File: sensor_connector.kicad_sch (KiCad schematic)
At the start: 4 parts

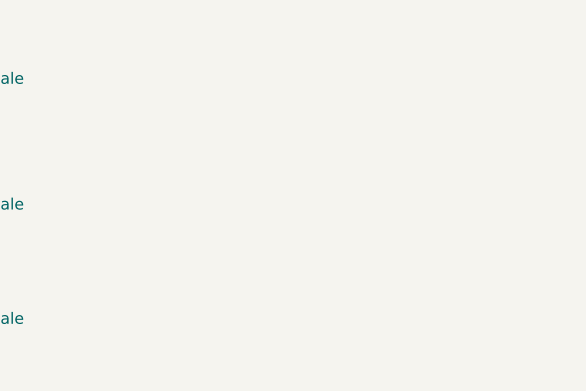
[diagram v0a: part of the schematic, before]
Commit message: Added Amplifier board om "special" lib. Added Amplifier to board with shutdown pins. Added DHT11 sensor to sensor schematic. Updated connector lib.
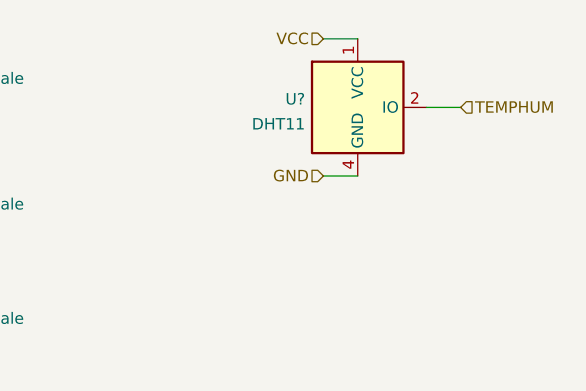
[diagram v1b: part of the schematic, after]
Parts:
- added U?: DHT11, Sensor:Aosong_DHT11_5.5x12.0_P2.54mm, symbol Sensor:DHT11
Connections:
- net GND: now also U?.4 (GND)
- net VCC: now also U?.1 (VCC)
- new net TEMPHUM: U?.2 (IO)
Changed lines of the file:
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@@
 (kicad_sch (version 20211123) (generator eeschema)
   (paper "A4")
+  (wire (pts (xy 156.21 54.61) (xy 152.4 54.61))
+    (stroke (width 0) (type default) (color 0 0 0 0))
+  )
   (wire (pts (xy 83.82 60.96) (xy 80.01 60.96))
     (stroke (width 0) (type default) (color 0 0 0 0))
@@
   )
   (wire (pts (xy 80.01 63.5) (xy 83.82 63.5))
+    (stroke (width 0) (type default) (color 0 0 0 0))
+  )
+  (wire (pts (xy 144.78 62.23) (xy 140.97 62.23))
     (stroke (width 0) (type default) (color 0 0 0 0))
   )
@@
     (stroke (width 0) (type default) (color 0 0 0 0))
   )
+  (wire (pts (xy 144.78 46.99) (xy 140.97 46.99))
+    (stroke (width 0) (type default) (color 0 0 0 0))
+  )
   (hierarchical_label "GND" (shape input) (at 80.01 78.74 180)
     (effects (font (size 1.27 1.27)) (justify right))
@@
   )
   (hierarchical_label "GND" (shape input) (at 80.01 66.04 180)
+    (effects (font (size 1.27 1.27)) (justify right))
+  )
+  (hierarchical_label "VCC" (shape input) (at 140.97 46.99 180)
+    (effects (font (size 1.27 1.27)) (justify right))
+  )
+  (hierarchical_label "TEMPHUM" (shape input) (at 156.21 54.61 0)
+    (effects (font (size 1.27 1.27)) (justify left))
+  )
+  (hierarchical_label "GND" (shape input) (at 140.97 62.23 180)
     (effects (font (size 1.27 1.27)) (justify right))
   )
@@
     (pin "3")
   )
+  (symbol (lib_id "Sensor:DHT11") (at 144.78 54.61 0) (unit 1)
+    (in_bom yes) (on_board yes) (fields_autoplaced)
+    (property "Reference" "U?" (id 0) (at 138.9381 53.7015 0)
+      (effects (font (size 1.27 1.27)) (justify right))
+    )
+    (property "Value" "DHT11" (id 1) (at 138.9381 56.4766 0)
+      (effects (font (size 1.27 1.27)) (justify right))
+    )
+    (property "Footprint" "Sensor:Aosong_DHT11_5.5x12.0_P2.54mm" (id 2) (at 144.78 64.77 0)
+      (effects (font (size 1.27 1.27)) hide)
+    )
+    (property "Datasheet" "http://akizukidenshi.com/download/ds/aosong/DHT11.pdf" (id 3) (at 148.59 48.26 0)
+      (effects (font (size 1.27 1.27)) hide)
+    )
+    (pin "1")
+    (pin "2")
+    (pin "3")
+    (pin "4")
+  )
   (symbol (lib_id "Connector:Conn_01x03_Female") (at 88.9 63.5 0) (unit 1)

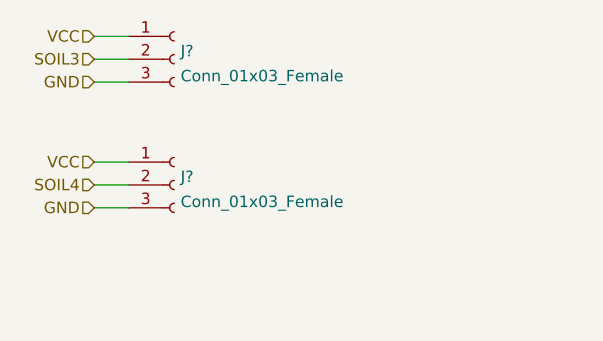
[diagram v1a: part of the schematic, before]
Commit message: Corrected RESET curcit to not keep the device in reset state. Added more capacitors to be a buffer for the motor. Added fuse to motor.
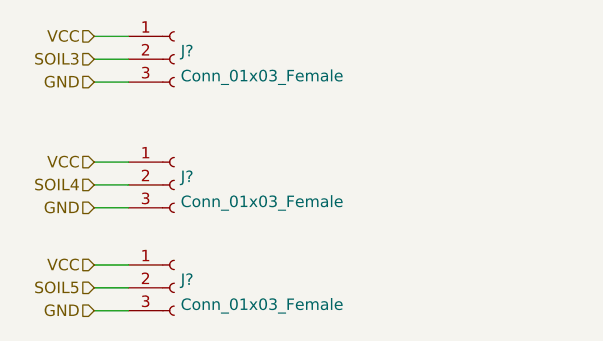
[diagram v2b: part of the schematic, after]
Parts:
- added J?: Conn_01x03_Female, symbol Connector:Conn_01x03_Female
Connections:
- net GND: now also J?.3 (Pin_3)
- net VCC: now also J?.1 (Pin_1)
- new net SOIL5: J?.2 (Pin_2)
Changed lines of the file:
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@@
+    (stroke (width 0) (type default) (color 0 0 0 0))
+  )
+  (wire (pts (xy 83.82 99.06) (xy 80.01 99.06))
     (stroke (width 0) (type default) (color 0 0 0 0))
   )
   (wire (pts (xy 80.01 63.5) (xy 83.82 63.5))
+    (stroke (width 0) (type default) (color 0 0 0 0))
+  )
+  (wire (pts (xy 83.82 104.14) (xy 80.01 104.14))
     (stroke (width 0) (type default) (color 0 0 0 0))
   )
@@
     (stroke (width 0) (type default) (color 0 0 0 0))
   )
+  (wire (pts (xy 80.01 101.6) (xy 83.82 101.6))
+    (stroke (width 0) (type default) (color 0 0 0 0))
+  )
   (wire (pts (xy 80.01 76.2) (xy 83.82 76.2))
     (stroke (width 0) (type default) (color 0 0 0 0))
@@
   (wire (pts (xy 144.78 46.99) (xy 140.97 46.99))
     (stroke (width 0) (type default) (color 0 0 0 0))
+  )
+  (hierarchical_label "SOIL5" (shape input) (at 80.01 101.6 180)
+    (effects (font (size 1.27 1.27)) (justify right))
   )
   (hierarchical_label "GND" (shape input) (at 80.01 78.74 180)
@@
     (effects (font (size 1.27 1.27)) (justify right))
   )
+  (hierarchical_label "VCC" (shape input) (at 80.01 99.06 180)
+    (effects (font (size 1.27 1.27)) (justify right))
+  )
   (hierarchical_label "GND" (shape input) (at 80.01 52.07 180)
     (effects (font (size 1.27 1.27)) (justify right))
   )
   (hierarchical_label "VCC" (shape input) (at 80.01 73.66 180)
+    (effects (font (size 1.27 1.27)) (justify right))
+  )
+  (hierarchical_label "GND" (shape input) (at 80.01 104.14 180)
     (effects (font (size 1.27 1.27)) (justify right))
   )
@@
       (effects (font (size 1.27 1.27)) hide)
     )
+    (pin "1")
+    (pin "2")
+    (pin "3")
+  )
+  (symbol (lib_id "Connector:Conn_01x03_Female") (at 88.9 101.6 0) (unit 1)
+    (in_bom yes) (on_board yes) (fields_autoplaced)
+    (property "Reference" "J?" (id 0) (at 89.6112 100.6915 0)
+      (effects (font (size 1.27 1.27)) (justify left))
+    )
+    (property "Value" "Conn_01x03_Female" (id 1) (at 89.6112 103.4666 0)
+      (effects (font (size 1.27 1.27)) (justify left))
+    )
+    (property "Footprint" "" (id 2) (at 88.9 101.6 0)
+      (effects (font (size 1.27 1.27)) hide)
+    )
+    (property "Datasheet" "~" (id 3) (at 88.9 101.6 0)
+      (effects (font (size 1.27 1.27)) hide)
+    )

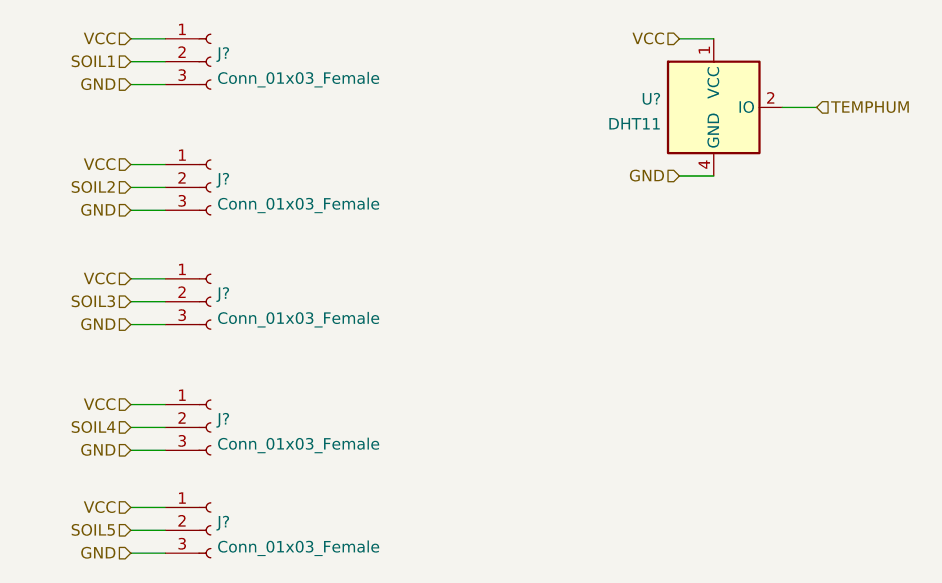
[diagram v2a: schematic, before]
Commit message: Added pcb, not routed but sorted. Gave all footprints refernces. Missing some footprints or might be wrong.
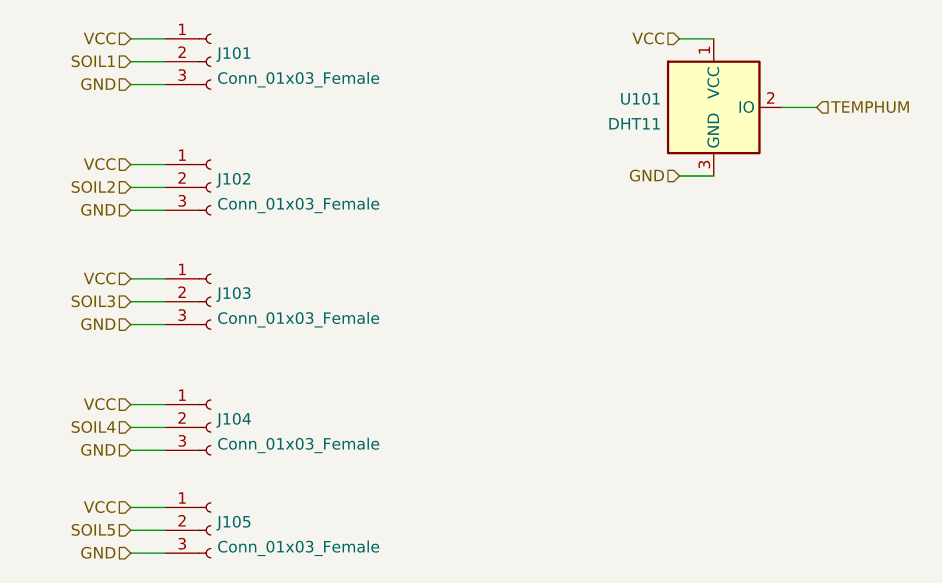
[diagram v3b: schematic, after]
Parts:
- J101, J102, J103, J104, J105: renamed from J?; footprint (none) -> Connector_JST:JST_XH_B3B-XH-A_1x03_P2.50mm_Vertical
- U101: renamed from U?; footprint Sensor:Aosong_DHT11_5.5x12.0_P2.54mm -> Connector_PinSocket_2.54mm:PinSocket_1x03_P2.54mm_Vertical; symbol Sensor:DHT11 -> special:DHT11
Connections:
- net GND: now also U101.3 (GND); no longer U101.4 (GND)
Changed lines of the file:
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@@
   (symbol (lib_id "Connector:Conn_01x03_Female") (at 88.9 90.17 0) (unit 1)
     (in_bom yes) (on_board yes) (fields_autoplaced)
-    (property "Reference" "J?" (id 0) (at 89.6112 89.2615 0)
+    (property "Reference" "J104" (id 0) (at 89.6112 89.2615 0)
       (effects (font (size 1.27 1.27)) (justify left))
     )
@@
       (effects (font (size 1.27 1.27)) (justify left))
     )
-    (property "Footprint" "" (id 2) (at 88.9 90.17 0)
+    (property "Footprint" "Connector_JST:JST_XH_B3B-XH-A_1x03_P2.50mm_Vertical" (id 2) (at 88.9 90.17 0)
       (effects (font (size 1.27 1.27)) hide)
     )
@@
   (symbol (lib_id "Connector:Conn_01x03_Female") (at 88.9 101.6 0) (unit 1)
     (in_bom yes) (on_board yes) (fields_autoplaced)
-    (property "Reference" "J?" (id 0) (at 89.6112 100.6915 0)
+    (property "Reference" "J105" (id 0) (at 89.6112 100.6915 0)
       (effects (font (size 1.27 1.27)) (justify left))
     )
@@
       (effects (font (size 1.27 1.27)) (justify left))
     )
-    (property "Footprint" "" (id 2) (at 88.9 101.6 0)
+    (property "Footprint" "Connector_JST:JST_XH_B3B-XH-A_1x03_P2.50mm_Vertical" (id 2) (at 88.9 101.6 0)
       (effects (font (size 1.27 1.27)) hide)
     )
@@
     (pin "3")
   )
-  (symbol (lib_id "Sensor:DHT11") (at 144.78 54.61 0) (unit 1)
+  (symbol (lib_id "special:DHT11") (at 144.78 54.61 0) (unit 1)
     (in_bom yes) (on_board yes) (fields_autoplaced)
-    (property "Reference" "U?" (id 0) (at 138.9381 53.7015 0)
+    (property "Reference" "U101" (id 0) (at 138.9381 53.7015 0)
       (effects (font (size 1.27 1.27)) (justify right))
     )
@@
       (effects (font (size 1.27 1.27)) (justify right))
     )
-    (property "Footprint" "Sensor:Aosong_DHT11_5.5x12.0_P2.54mm" (id 2) (at 144.78 64.77 0)
+    (property "Footprint" "Connector_PinSocket_2.54mm:PinSocket_1x03_P2.54mm_Vertical" (id 2) (at 144.78 64.77 0)
       (effects (font (size 1.27 1.27)) hide)
     )
@@
     (pin "2")
     (pin "3")
-    (pin "4")
   )
   (symbol (lib_id "Connector:Conn_01x03_Female") (at 88.9 63.5 0) (unit 1)
     (in_bom yes) (on_board yes) (fields_autoplaced)
-    (property "Reference" "J?" (id 0) (at 89.6112 62.5915 0)
+    (property "Reference" "J102" (id 0) (at 89.6112 62.5915 0)
       (effects (font (size 1.27 1.27)) (justify left))
     )
@@
       (effects (font (size 1.27 1.27)) (justify left))
     )
-    (property "Footprint" "" (id 2) (at 88.9 63.5 0)
+    (property "Footprint" "Connector_JST:JST_XH_B3B-XH-A_1x03_P2.50mm_Vertical" (id 2) (at 88.9 63.5 0)
       (effects (font (size 1.27 1.27)) hide)
     )
@@
   (symbol (lib_id "Connector:Conn_01x03_Female") (at 88.9 76.2 0) (unit 1)
     (in_bom yes) (on_board yes) (fields_autoplaced)
-    (property "Reference" "J?" (id 0) (at 89.6112 75.2915 0)
+    (property "Reference" "J103" (id 0) (at 89.6112 75.2915 0)
       (effects (font (size 1.27 1.27)) (justify left))
     )
@@
       (effects (font (size 1.27 1.27)) (justify left))
     )
-    (property "Footprint" "" (id 2) (at 88.9 76.2 0)
+    (property "Footprint" "Connector_JST:JST_XH_B3B-XH-A_1x03_P2.50mm_Vertical" (id 2) (at 88.9 76.2 0)
       (effects (font (size 1.27 1.27)) hide)
     )
@@
   (symbol (lib_id "Connector:Conn_01x03_Female") (at 88.9 49.53 0) (unit 1)
     (in_bom yes) (on_board yes) (fields_autoplaced)
-    (property "Reference" "J?" (id 0) (at 89.6112 48.6215 0)
+    (property "Reference" "J101" (id 0) (at 89.6112 48.6215 0)
       (effects (font (size 1.27 1.27)) (justify left))
     )
@@
       (effects (font (size 1.27 1.27)) (justify left))
     )
-    (property "Footprint" "" (id 2) (at 88.9 49.53 0)
+    (property "Footprint" "Connector_JST:JST_XH_B3B-XH-A_1x03_P2.50mm_Vertical" (id 2) (at 88.9 49.53 0)
       (effects (font (size 1.27 1.27)) hide)
     )

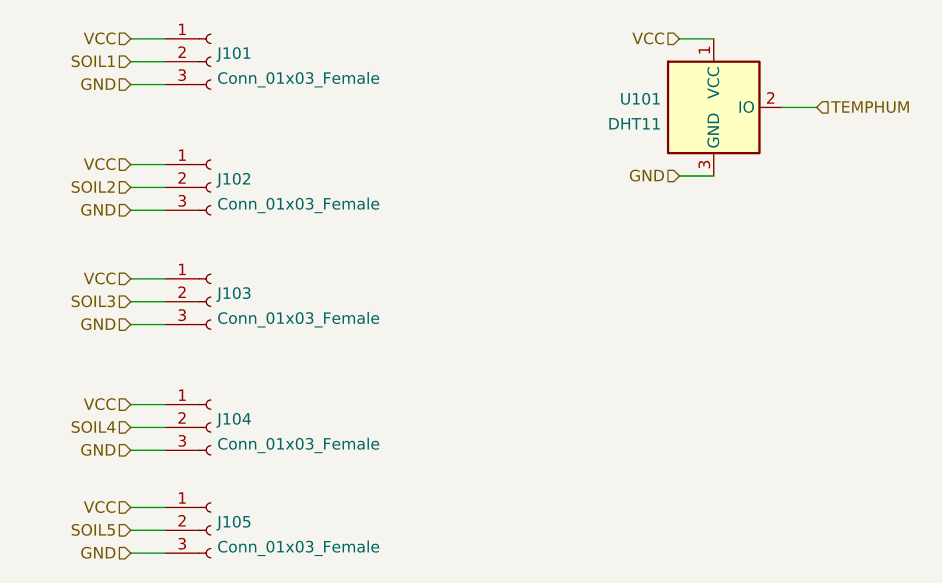
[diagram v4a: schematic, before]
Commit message: Renamed ConnectorEsp folder so 3D models work. Started routing and more layout work.
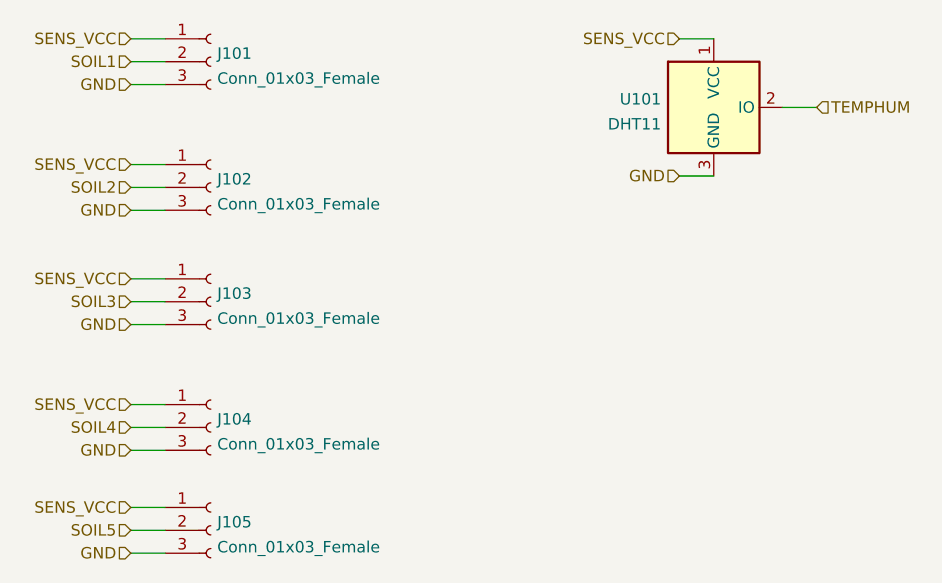
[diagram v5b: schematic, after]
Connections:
- net VCC renamed SENS_VCC
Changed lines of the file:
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@@
     (effects (font (size 1.27 1.27)) (justify right))
   )
-  (hierarchical_label "VCC" (shape input) (at 80.01 99.06 180)
+  (hierarchical_label "SENS_VCC" (shape input) (at 80.01 99.06 180)
     (effects (font (size 1.27 1.27)) (justify right))
   )
@@
     (effects (font (size 1.27 1.27)) (justify right))
   )
-  (hierarchical_label "VCC" (shape input) (at 80.01 73.66 180)
+  (hierarchical_label "SENS_VCC" (shape input) (at 80.01 73.66 180)
     (effects (font (size 1.27 1.27)) (justify right))
   )
@@
     (effects (font (size 1.27 1.27)) (justify right))
   )
-  (hierarchical_label "VCC" (shape input) (at 140.97 46.99 180)
+  (hierarchical_label "SENS_VCC" (shape input) (at 140.97 46.99 180)
     (effects (font (size 1.27 1.27)) (justify right))
   )
@@
     (effects (font (size 1.27 1.27)) (justify right))
   )
-  (hierarchical_label "VCC" (shape input) (at 80.01 87.63 180)
+  (hierarchical_label "SENS_VCC" (shape input) (at 80.01 87.63 180)
     (effects (font (size 1.27 1.27)) (justify right))
   )
-  (hierarchical_label "VCC" (shape input) (at 80.01 46.99 180)
+  (hierarchical_label "SENS_VCC" (shape input) (at 80.01 46.99 180)
     (effects (font (size 1.27 1.27)) (justify right))
   )
-  (hierarchical_label "VCC" (shape input) (at 80.01 60.96 180)
+  (hierarchical_label "SENS_VCC" (shape input) (at 80.01 60.96 180)
     (effects (font (size 1.27 1.27)) (justify right))
   )
